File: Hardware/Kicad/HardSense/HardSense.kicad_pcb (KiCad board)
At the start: 2 copper layers, 60.3 x 56.5 mm, 12 parts, among them J1 Conn_01x02, U1 ESP32-DEVKITC-32D

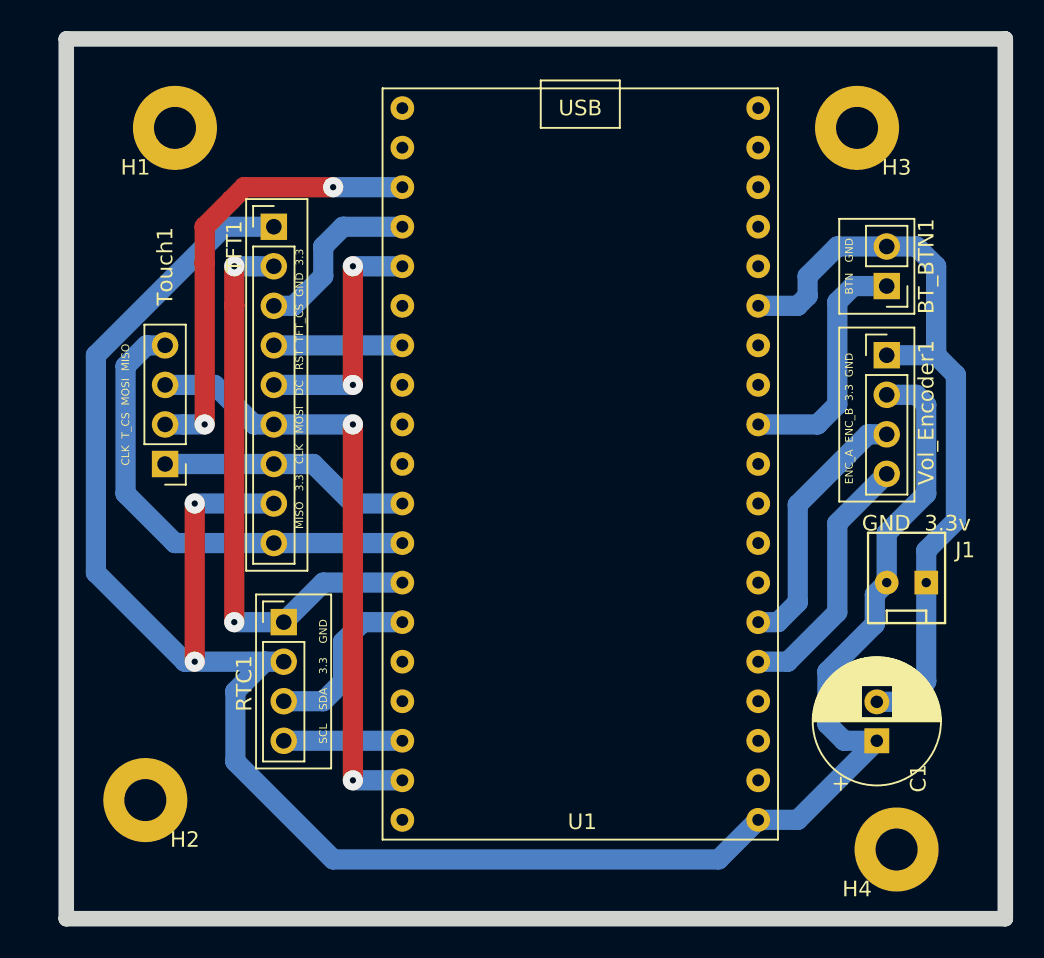
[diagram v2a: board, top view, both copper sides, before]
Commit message: Some minor updates to the pcb
Moving stuff around as I'm going to create a new KiCad project for the
NodeMCU-32S board
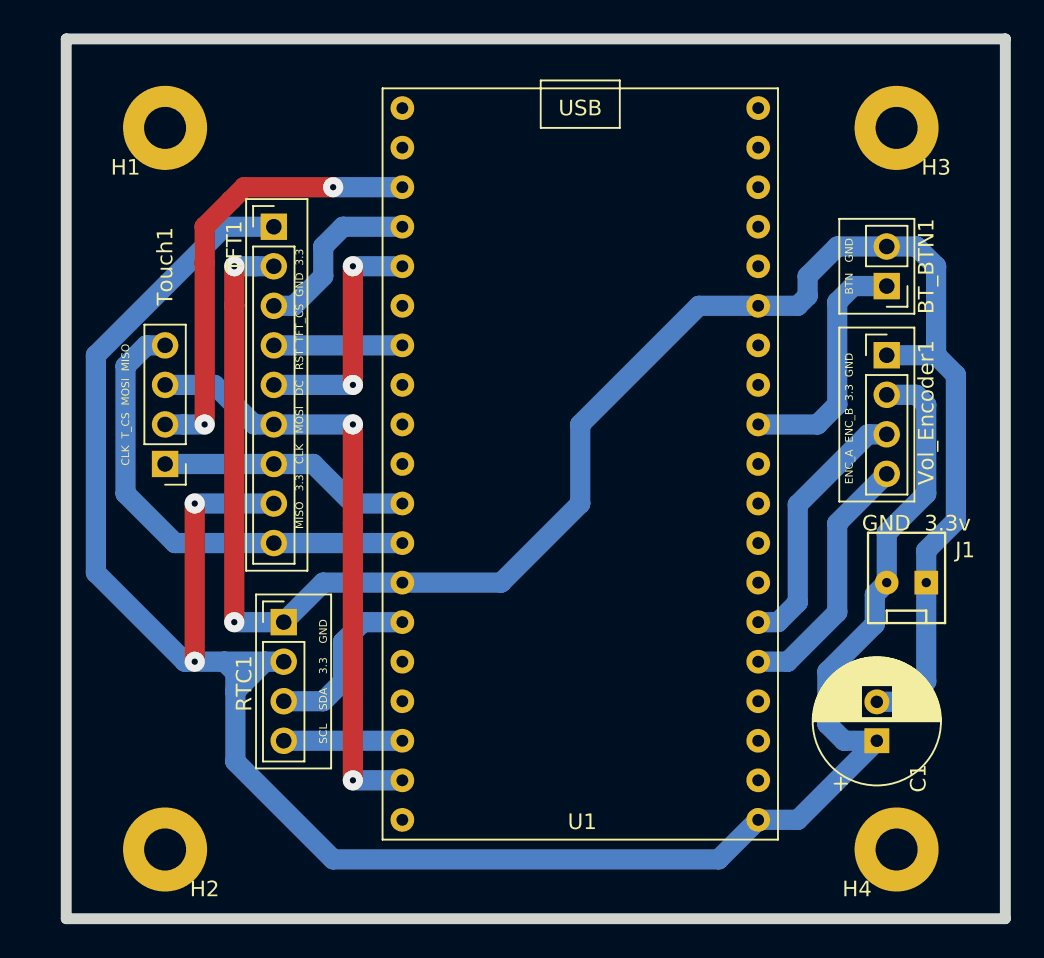
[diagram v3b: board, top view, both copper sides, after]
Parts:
- moved H2 3.42 mm to (114.3, 106.0)
- moved H3 2.54 mm to (161.3, 59.7)
- moved H1 0.64 mm to (114.3, 59.7)
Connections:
- BT_BTN1 pad 2: GNDA -> GND
- C1 pad 2: GNDA -> GND
- J1 pad 1: GNDA -> GND
- U1 pad 14: GNDA -> GND
- Vol_Encoder1 pad 1: GNDA -> GND
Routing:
- net GND: track 37.2 -> 119.6 mm
- net GNDA: track 49.2 -> 0.00 mm
- net 3.3V: track 142.2 -> 144.4 mm
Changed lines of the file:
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@@
     (thickness 1.6)
     (drawings 33)
-    (tracks 114)
+    (tracks 122)
     (zones 0)
     (modules 12)
-    (nets 39)
+    (nets 38)
   )
   (page A4)
@@
   (net 36 "Net-(U1-Pad2)")
   (net 37 "Net-(U1-Pad7)")
-  (net 38 GNDA)
   (net_class Default "This is the default net class."
     (clearance 0.2)
@@
     (add_net 3.3V)
     (add_net GND)
-    (add_net GNDA)
     (add_net "Net-(U1-Pad10)")
     (add_net "Net-(U1-Pad12)")
@@
       (net 28 "Net-(U1-Pad15)"))
     (pad 14 thru_hole circle (at -11.43 10.16 180) (size 1.524 1.524) (drill 0.762) (layers *.Cu *.Mask)
-      (net 38 GNDA))
+      (net 1 GND))
     (pad 13 thru_hole circle (at -11.43 7.62 180) (size 1.524 1.524) (drill 0.762) (layers *.Cu *.Mask)
       (net 29 "Net-(U1-Pad13)"))
@@
     (fp_circle (center 1.25 0) (end 5.25 0) (layer F.Fab) (width 0.1))
     (pad 2 thru_hole circle (at 2.5 0 90) (size 1.6 1.6) (drill 0.8) (layers *.Cu *.Mask)
-      (net 38 GNDA))
+      (net 1 GND))
     (pad 1 thru_hole rect (at 0 0 90) (size 1.6 1.6) (drill 0.8) (layers *.Cu *.Mask)
       (net 2 3.3V))
@@
   )
   (module MountingHole:MountingHole_2.7mm_Pad (layer F.Cu)
-    (at 158.75 59.69)
+    (at 161.29 59.69)
     (descr "Mounting Hole 2.7mm")
     (tags "mounting hole 2.7mm")
@@
   )
   (module MountingHole:MountingHole_2.7mm_Pad (layer F.Cu)
-    (at 113.03 102.87)
+    (at 114.3 106.045)
     (descr "Mounting Hole 2.7mm")
     (tags "mounting hole 2.7mm")
@@
   )
   (module MountingHole:MountingHole_2.7mm_Pad (layer F.Cu)
-    (at 114.935 59.69)
+    (at 114.3 59.69)
     (descr "Mounting Hole 2.7mm")
     (tags "mounting hole 2.7mm")
@@
       (net 2 3.3V))
     (pad 1 thru_hole rect (at 0 0) (size 1.7 1.7) (drill 1) (layers *.Cu *.Mask)
-      (net 38 GNDA))
+      (net 1 GND))
     (model ${KISYS3DMOD}/Connector_PinHeader_2.54mm.3dshapes/PinHeader_1x04_P2.54mm_Vertical.wrl
       (at (xyz 0 0 0))
@@
       (net 2 3.3V))
     (pad 1 thru_hole rect (at 0 -2.54 270) (size 1.524 1.524) (drill 0.6) (layers *.Cu *.Mask)
-      (net 38 GNDA))
+      (net 1 GND))
     (model :Kitecraft_Pin_Headers_3D:PinHeader_1x02_P2.54_Friction_Lock.step
       (offset (xyz 0 1.28 3.3))
@@
     (fp_line (start -0.635 -1.27) (end 1.27 -1.27) (layer F.Fab) (width 0.1))
     (pad 2 thru_hole oval (at 0 2.54 180) (size 1.7 1.7) (drill 1) (layers *.Cu *.Mask)
-      (net 38 GNDA))
+      (net 1 GND))
     (pad 1 thru_hole rect (at 0 0 180) (size 1.7 1.7) (drill 1) (layers *.Cu *.Mask)
       (net 12 /BT_BTN))
@@
     )
   )
-  (gr_line (start 107.95 53.975) (end 168.275 53.975) (layer Edge.Cuts) (width 1))
-  (gr_line (start 107.95 110.49) (end 107.95 53.975) (layer Edge.Cuts) (width 1))
+  (gr_line (start 107.95 53.975) (end 168.275 53.975) (layer Edge.Cuts) (width 0.7))
+  (gr_line (start 107.95 110.49) (end 107.95 53.975) (layer Edge.Cuts) (width 0.7))
   (gr_text "GND  3.3v" (at 162.56 85.09) (layer F.SilkS)
     (effects (font (size 1 1) (thickness 0.15)))
@@
     (effects (font (size 0.5 0.5) (thickness 0.125)))
   )
-  (gr_line (start 168.275 110.49) (end 168.275 53.975) (layer Edge.Cuts) (width 1))
-  (gr_line (start 107.95 110.49) (end 168.275 110.49) (layer Edge.Cuts) (width 1))
+  (gr_line (start 168.275 110.49) (end 168.275 53.975) (layer Edge.Cuts) (width 0.7))
+  (gr_line (start 107.95 110.49) (end 168.275 110.49) (layer Edge.Cuts) (width 0.7))
   (gr_text "BTN   GND" (at 158.242 68.58 90) (layer F.SilkS)
     (effects (font (size 0.5 0.5) (thickness 0.125)))
@@
   (segment (start 162.56 76.835) (end 160.655 76.835) (width 1.3) (layer B.Cu) (net 2))
   (segment (start 163.195 77.47) (end 162.56 76.835) (width 1.3) (layer B.Cu) (net 2))
-  (segment (start 120.717919 93.98) (end 118.812919 95.885) (width 1.3) (layer B.Cu) (net 2))
   (segment (start 121.92 93.98) (end 120.717919 93.98) (width 1.3) (layer B.Cu) (net 2))
   (segment (start 118.812919 95.885) (end 118.812919 100.397919) (width 1.3) (layer B.Cu) (net 2))
@@
   (segment (start 116.205 83.82) (end 116.205 93.98) (width 1.3) (layer F.Cu) (net 2))
   (via (at 116.205 93.98) (size 1.3) (drill 0.4) (layers F.Cu B.Cu) (net 2))
-  (segment (start 115.57 93.98) (end 120.717919 93.98) (width 1.3) (layer B.Cu) (net 2))
   (segment (start 109.855 88.265) (end 115.57 93.98) (width 1.3) (layer B.Cu) (net 2))
   (segment (start 109.855 74.295) (end 109.855 88.265) (width 1.3) (layer B.Cu) (net 2))
@@
   (segment (start 125.73 92.71) (end 127 91.44) (width 1.3) (layer B.Cu) (net 14))
   (segment (start 127 91.44) (end 129.54 91.44) (width 1.3) (layer B.Cu) (net 14))
-  (segment (start 161.885 96.56) (end 160.02 96.56) (width 1.3) (layer B.Cu) (net 38))
-  (segment (start 163.195 88.9) (end 163.195 95.25) (width 1.3) (layer B.Cu) (net 38))
-  (segment (start 163.195 95.25) (end 161.885 96.56) (width 1.3) (layer B.Cu) (net 38))
-  (segment (start 163.195 86.838) (end 165.1 84.933) (width 1.3) (layer B.Cu) (net 38))
-  (segment (start 163.195 88.9) (end 163.195 86.838) (width 1.3) (layer B.Cu) (net 38))
-  (segment (start 165.1 84.933) (end 165.1 75.565) (width 1.3) (layer B.Cu) (net 38))
-  (segment (start 163.83 74.295) (end 160.655 74.295) (width 1.3) (layer B.Cu) (net 38))
-  (segment (start 165.1 75.565) (end 163.83 74.295) (width 1.3) (layer B.Cu) (net 38))
-  (segment (start 160.655 67.31) (end 162.56 67.31) (width 1.3) (layer B.Cu) (net 38))
-  (segment (start 163.83 68.58) (end 163.83 74.295) (width 1.3) (layer B.Cu) (net 38))
-  (segment (start 162.56 67.31) (end 163.83 68.58) (width 1.3) (layer B.Cu) (net 38))
-  (segment (start 160.655 67.31) (end 157.48 67.31) (width 1.3) (layer B.Cu) (net 38))
-  (segment (start 157.48 67.31) (end 155.575 69.215) (width 1.3) (layer B.Cu) (net 38))
-  (segment (start 155.575 69.215) (end 155.575 70.485) (width 1.3) (layer B.Cu) (net 38))
-  (segment (start 155.575 70.485) (end 154.94 71.12) (width 1.3) (layer B.Cu) (net 38))
-  (segment (start 154.94 71.12) (end 152.4 71.12) (width 1.3) (layer B.Cu) (net 38))
+  (segment (start 161.885 96.56) (end 160.02 96.56) (width 1.3) (layer B.Cu) (net 1))
+  (segment (start 163.195 88.9) (end 163.195 95.25) (width 1.3) (layer B.Cu) (net 1))
+  (segment (start 163.195 95.25) (end 161.885 96.56) (width 1.3) (layer B.Cu) (net 1))
+  (segment (start 163.195 86.838) (end 165.1 84.933) (width 1.3) (layer B.Cu) (net 1))
+  (segment (start 163.195 88.9) (end 163.195 86.838) (width 1.3) (layer B.Cu) (net 1))
+  (segment (start 165.1 84.933) (end 165.1 75.565) (width 1.3) (layer B.Cu) (net 1))
+  (segment (start 163.83 74.295) (end 160.655 74.295) (width 1.3) (layer B.Cu) (net 1))
+  (segment (start 165.1 75.565) (end 163.83 74.295) (width 1.3) (layer B.Cu) (net 1))
+  (segment (start 160.655 67.31) (end 162.56 67.31) (width 1.3) (layer B.Cu) (net 1))
+  (segment (start 163.83 68.58) (end 163.83 74.295) (width 1.3) (layer B.Cu) (net 1))
+  (segment (start 162.56 67.31) (end 163.83 68.58) (width 1.3) (layer B.Cu) (net 1))
+  (segment (start 160.655 67.31) (end 157.48 67.31) (width 1.3) (layer B.Cu) (net 1))
+  (segment (start 157.48 67.31) (end 155.575 69.215) (width 1.3) (layer B.Cu) (net 1))
+  (segment (start 155.575 69.215) (end 155.575 70.485) (width 1.3) (layer B.Cu) (net 1))
+  (segment (start 155.575 70.485) (end 154.94 71.12) (width 1.3) (layer B.Cu) (net 1))
+  (segment (start 154.94 71.12) (end 152.4 71.12) (width 1.3) (layer B.Cu) (net 1))
+  (segment (start 135.89 88.9) (end 129.54 88.9) (width 1.3) (layer B.Cu) (net 1))
+  (segment (start 140.97 83.82) (end 135.89 88.9) (width 1.3) (layer B.Cu) (net 1))
+  (segment (start 140.97 78.74) (end 140.97 83.82) (width 1.3) (layer B.Cu) (net 1))
+  (segment (start 152.4 71.12) (end 148.59 71.12) (width 1.3) (layer B.Cu) (net 1))
+  (segment (start 148.59 71.12) (end 140.97 78.74) (width 1.3) (layer B.Cu) (net 1))
+  (segment (start 120.717919 93.98) (end 118.812919 95.885) (width 1.3) (layer B.Cu) (net 2))
+  (segment (start 118.812919 94.682919) (end 118.11 93.98) (width 1.3) (layer B.Cu) (net 2))
+  (segment (start 118.812919 95.885) (end 118.812919 94.682919) (width 1.3) (layer B.Cu) (net 2))
+  (segment (start 115.57 93.98) (end 118.11 93.98) (width 1.3) (layer B.Cu) (net 2))
+  (segment (start 118.11 93.98) (end 120.717919 93.98) (width 1.3) (layer B.Cu) (net 2))
 )

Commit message: New KiCad schematic and PCB for ESP32S based system. Updated code with new pin mappings for ESP32S based sytem.
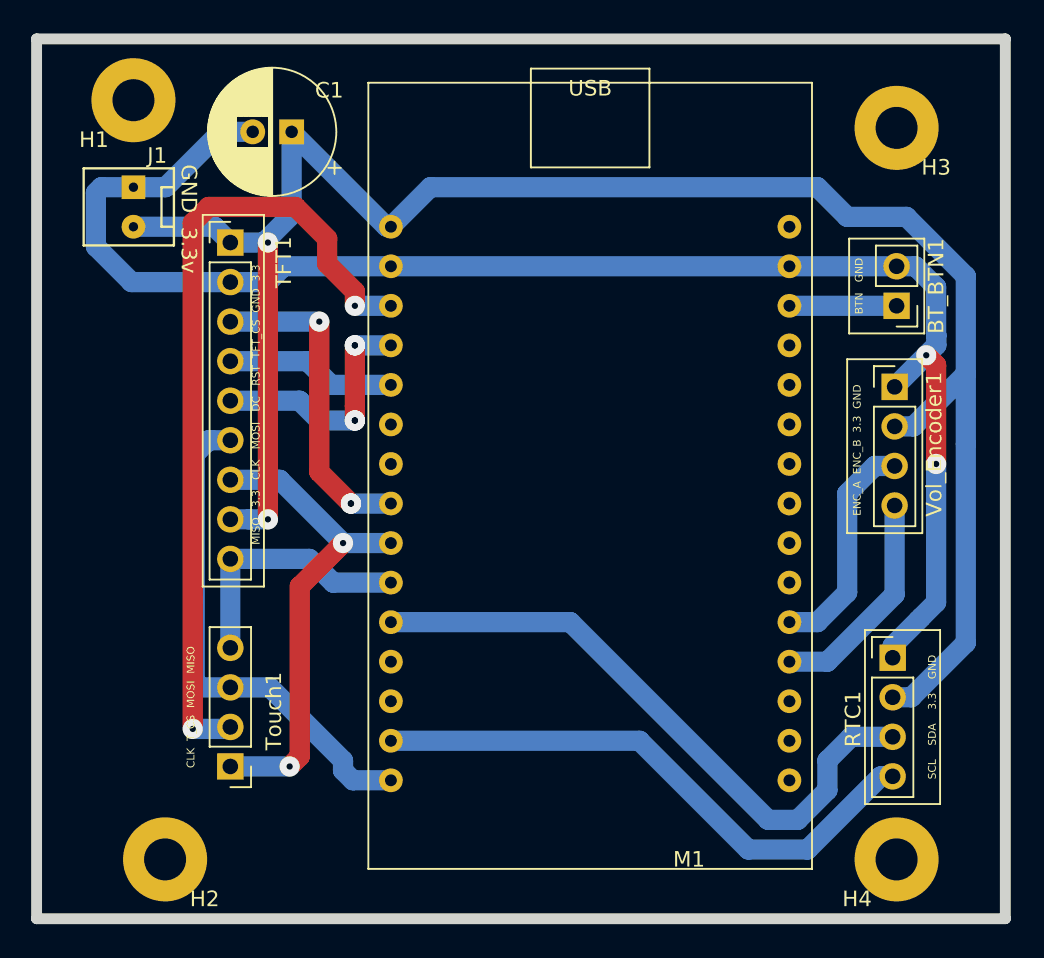
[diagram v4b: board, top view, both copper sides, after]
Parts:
- removed U1: ESP32-DEVKITC-32D, Kitecraft_Boards:NodeMCU_ESP-32S_38_Pin
- added M1: ESP32_DevKitC-30Pin, Kitecraft_Boards:ESP32S_30Pin, F.Cu at (141.6, 83.8)
- moved C1 54.3 mm to (122.4, 59.9), turned to 180 degrees
- moved J1 53.5 mm to (112.3, 66.0), turned to 0 degrees
- moved RTC1 39.2 mm to (161.0, 93.7)
- moved Touch1 19.9 mm to (118.5, 100.7)
- moved TFT1 2.97 mm to (118.5, 67.1)
- moved H1 2.70 mm to (112.3, 57.9)
- moved Vol_Encoder1 2.09 mm to (161.2, 76.3)
- moved BT_BTN1 1.42 mm to (161.3, 71.1)
- moved H2 0.64 mm to (114.3, 106.7)
- moved H4 0.64 mm to (161.3, 106.7)
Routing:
- net /SCL: track 7.62 -> 37.1 mm
- net /SDA: track 11.6 -> 40.8 mm
- net /T_CS: track 29.0 -> 52.2 mm
- net 3.3V: track 144.4 -> 121.8 mm
- net GND: track 119.6 -> 99.4 mm
- net /SPI_CLK: track 16.3 -> 31.6 mm, vias 0 -> 2
- net /SPI_MISO: track 30.4 -> 16.7 mm
- net /TFT_CS: track 11.5 -> 20.8 mm, vias 0 -> 3
- net /BT_BTN: track 15.8 -> 6.88 mm
- net /SPI_MOSI: track 39.2 -> 32.9 mm, vias 2 -> 0
- net /TFT_RST: track 8.25 -> 10.9 mm
- net /ENC_A: track 16.6 -> 14.3 mm
- net /ENC_B: track 16.9 -> 14.6 mm
- net /TFT_DC: track 15.9 -> 15.7 mm, vias 2 -> 4
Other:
- board size 60.3 x 56.5 mm -> 62.2 x 56.5 mm
- board text removed: "USB"

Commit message: Updates to PCB board. Changed pin connections from ESP32S to TFT in order to get a better trace line on the PCB.
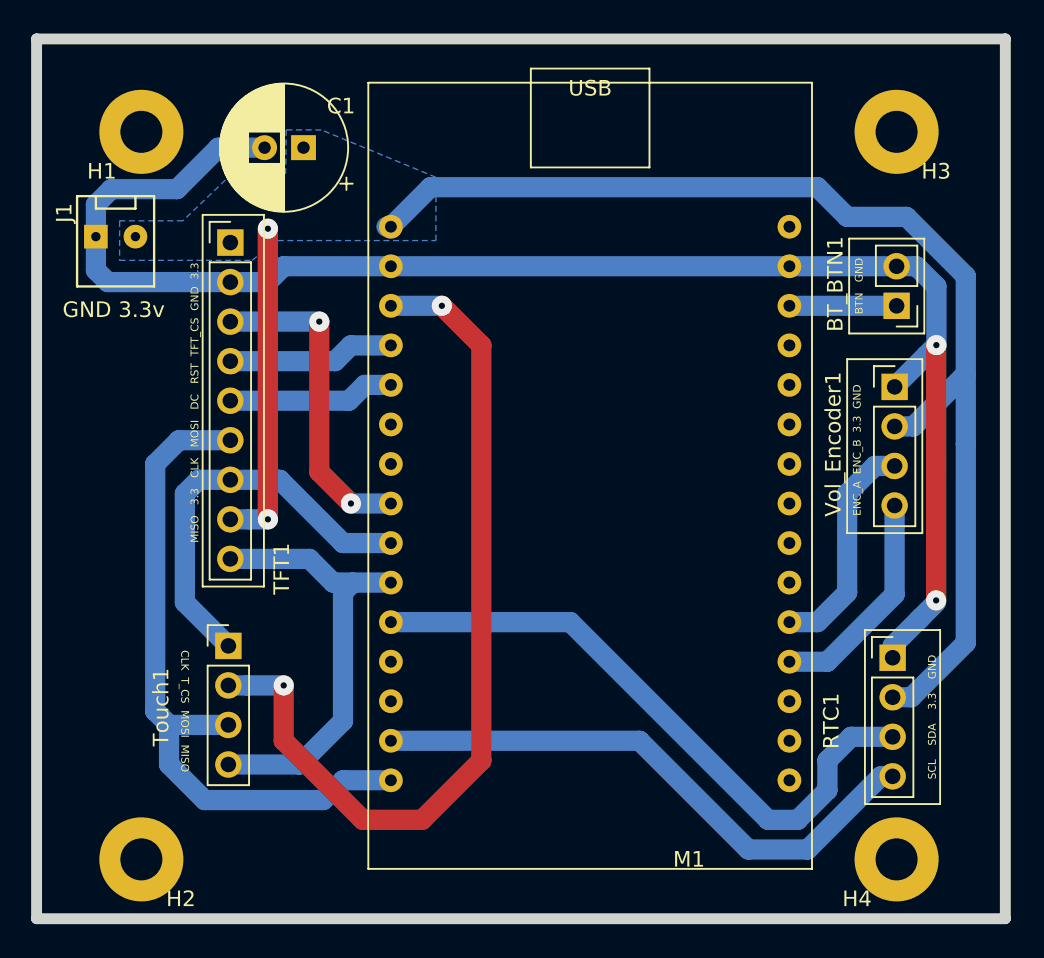
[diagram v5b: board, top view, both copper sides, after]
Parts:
- moved Touch1 7.75 mm to (118.4, 93.0), turned to 0 degrees
- moved H1 2.09 mm to (112.8, 59.9)
- moved H2 1.52 mm to (112.8, 106.7)
- moved C1 1.27 mm to (123.2, 61.0)
- moved J1 0.65 mm to (112.4, 66.7), turned to 90 degrees
- moved H3 0.25 mm to (161.3, 59.9)
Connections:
- M1 pad 4: /TFT_DC -> /TFT_RST
- M1 pad 5: /TFT_RST -> /TFT_DC
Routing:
- net 3.3V: track 121.8 -> 97.4 mm
- net /SPI_MISO: track 16.7 -> 28.6 mm
- net /SPI_MOSI: track 32.9 -> 44.7 mm
- net /SPI_CLK: track 31.6 -> 26.2 mm, vias 2 -> 0
- net /T_CS: track 52.2 -> 57.2 mm
- net /TFT_DC: track 15.7 -> 10.7 mm, vias 4 -> 0
- net GND: track 99.4 -> 100.5 mm
- net /TFT_CS: vias 3 -> 2
- added copper zone on B.Cu, net 3.3V
